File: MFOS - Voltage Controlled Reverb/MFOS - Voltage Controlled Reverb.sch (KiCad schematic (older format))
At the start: 94 parts, among them J1 X6, J10 X5, J11 GND_Conn, J12 +12V_Conn, J13 -12V_Conn, J14 X4, J2 X9, J3 X10, J4 X7, J5 X8, J6 X11, J7 X1, J8 X2, J9 X3, Q1 2N3906, Q2 2N3906, U1 LM386, U2 LF411, U3 TL074, U4 LM13700, U5 TL072, U6 TL072

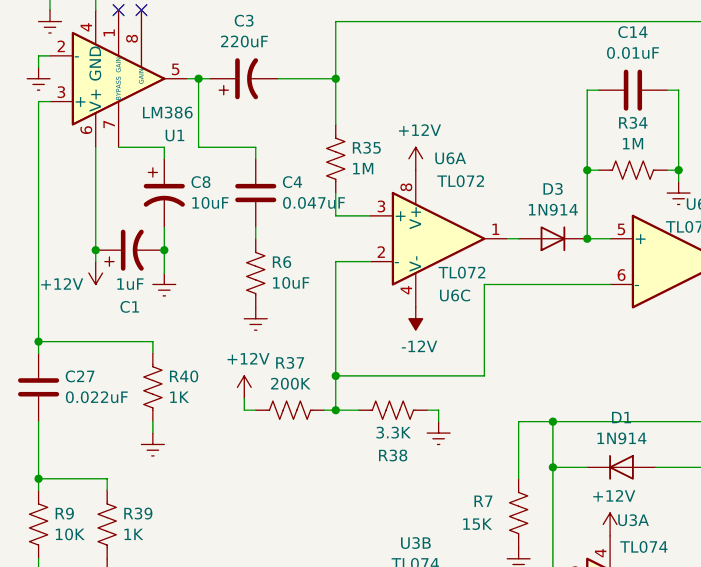
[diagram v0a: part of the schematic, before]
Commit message: placed components on pcb, some caps i think have the wrong footprint
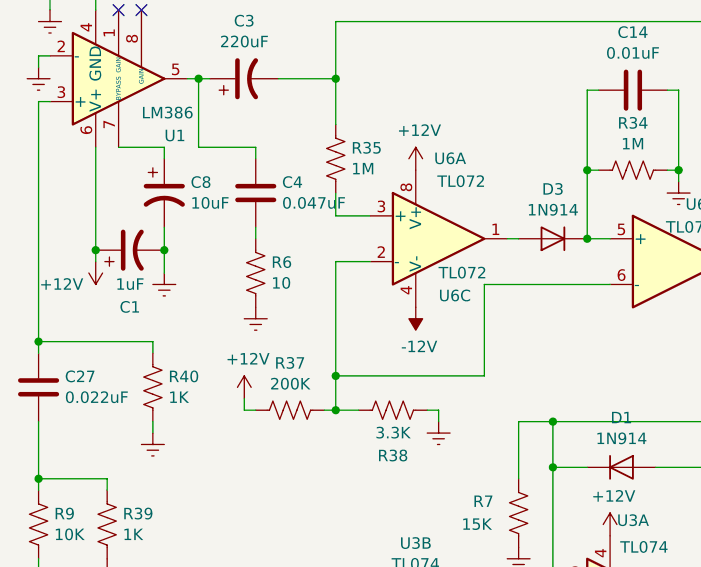
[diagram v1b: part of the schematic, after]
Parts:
- Q1, Q2: footprint Package_TO_SOT_THT:TO-92_Inline -> Package_TO_SOT_THT:TO-92_Inline_Wide
- R6: value 10uF -> 10
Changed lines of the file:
@@
 P 1650 1850
 F 0 "R6" H 1718 1896 50  0000 L CNN
-F 1 "10uF" H 1718 1805 50  0000 L CNN
+F 1 "10" H 1718 1805 50  0000 L CNN
 F 2 "Resistor_THT:R_Axial_DIN0207_L6.3mm_D2.5mm_P7.62mm_Horizontal" V 1690 1840 50  0001 C CNN
 F 3 "~" H 1650 1850 50  0001 C CNN
@@
 F 0 "Q1" H 4140 3254 50  0000 L CNN
 F 1 "2N3906" H 4140 3345 50  0000 L CNN
-F 2 "Package_TO_SOT_THT:TO-92_Inline" H 4150 3225 50  0001 L CIN
+F 2 "Package_TO_SOT_THT:TO-92_Inline_Wide" H 4150 3225 50  0001 L CIN
 F 3 "https://www.fairchildsemi.com/datasheets/2N/2N3906.pdf" H 3950 3300 50  0001 L CNN
 	1    3950 3300
@@
 F 0 "Q2" H 5090 6404 50  0000 L CNN
 F 1 "2N3906" H 5090 6495 50  0000 L CNN
-F 2 "Package_TO_SOT_THT:TO-92_Inline" H 5100 6375 50  0001 L CIN
+F 2 "Package_TO_SOT_THT:TO-92_Inline_Wide" H 5100 6375 50  0001 L CIN
 F 3 "https://www.fairchildsemi.com/datasheets/2N/2N3906.pdf" H 4900 6450 50  0001 L CNN
 	1    4900 6450

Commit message: progress on wiring
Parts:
- C1, C10, C11, C12, C13: footprint Capacitor_THT:C_Rect_L7.0mm_W2.5mm_P5.00mm -> Capacitor_THT:CP_Radial_D5.0mm_P2.50mm
- C26, C6, C7, C8, C9: footprint Capacitor_THT:CP_Radial_D8.0mm_P3.50mm -> Capacitor_THT:CP_Radial_D6.3mm_P2.50mm
- C3: footprint Capacitor_THT:C_Rect_L7.0mm_W2.5mm_P5.00mm -> Capacitor_THT:CP_Radial_D6.3mm_P2.50mm
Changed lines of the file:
@@
 F 0 "C1" V 850 1750 50  0000 C CNN
 F 1 "1uF" V 950 1750 50  0000 C CNN
-F 2 "Capacitor_THT:C_Rect_L7.0mm_W2.5mm_P5.00mm" H 1100 1750 50  0001 C CNN
+F 2 "Capacitor_THT:CP_Radial_D5.0mm_P2.50mm" H 1100 1750 50  0001 C CNN
 F 3 "~" H 1100 1750 50  0001 C CNN
 	1    1100 1750
@@
 F 0 "C3" V 1852 1000 50  0000 C CNN
 F 1 "220uF" V 1761 1000 50  0000 C CNN
-F 2 "Capacitor_THT:C_Rect_L7.0mm_W2.5mm_P5.00mm" H 1600 1000 50  0001 C CNN
+F 2 "Capacitor_THT:CP_Radial_D6.3mm_P2.50mm" H 1600 1000 50  0001 C CNN
 F 3 "~" H 1600 1000 50  0001 C CNN
 	1    1600 1000
@@
 F 0 "C10" V 6198 3950 50  0000 C CNN
 F 1 "1uF" V 6289 3950 50  0000 C CNN
-F 2 "Capacitor_THT:C_Rect_L7.0mm_W2.5mm_P5.00mm" H 6450 3950 50  0001 C CNN
+F 2 "Capacitor_THT:CP_Radial_D5.0mm_P2.50mm" H 6450 3950 50  0001 C CNN
 F 3 "~" H 6450 3950 50  0001 C CNN
 	1    6450 3950
@@
 F 0 "C12" V 6198 4350 50  0000 C CNN
 F 1 "1uF" V 6289 4350 50  0000 C CNN
-F 2 "Capacitor_THT:C_Rect_L7.0mm_W2.5mm_P5.00mm" H 6450 4350 50  0001 C CNN
+F 2 "Capacitor_THT:CP_Radial_D5.0mm_P2.50mm" H 6450 4350 50  0001 C CNN
 F 3 "~" H 6450 4350 50  0001 C CNN
 	1    6450 4350
@@
 F 0 "C9" V 7748 3850 50  0000 C CNN
 F 1 "10uF" V 7839 3850 50  0000 C CNN
-F 2 "Capacitor_THT:CP_Radial_D8.0mm_P3.50mm" H 8000 3850 50  0001 C CNN
+F 2 "Capacitor_THT:CP_Radial_D6.3mm_P2.50mm" H 8000 3850 50  0001 C CNN
 F 3 "~" H 8000 3850 50  0001 C CNN
 	1    8000 3850
@@
 F 0 "C8" H 1365 1546 50  0000 L CNN
 F 1 "10uF" H 1365 1455 50  0000 L CNN
-F 2 "Capacitor_THT:CP_Radial_D8.0mm_P3.50mm" H 1250 1500 50  0001 C CNN
+F 2 "Capacitor_THT:CP_Radial_D6.3mm_P2.50mm" H 1250 1500 50  0001 C CNN
 F 3 "~" H 1250 1500 50  0001 C CNN
 	1    1250 1500
@@
 F 0 "C7" V 9450 5750 50  0000 C CNN
 F 1 "220uF" V 9550 5750 50  0000 C CNN
-F 2 "Capacitor_THT:CP_Radial_D8.0mm_P3.50mm" H 9700 5750 50  0001 C CNN
+F 2 "Capacitor_THT:CP_Radial_D6.3mm_P2.50mm" H 9700 5750 50  0001 C CNN
 F 3 "~" H 9700 5750 50  0001 C CNN
 	1    9700 5750
@@
 F 0 "C6" V 8000 5750 50  0000 C CNN
 F 1 "220uF" V 8100 5750 50  0000 C CNN
-F 2 "Capacitor_THT:CP_Radial_D8.0mm_P3.50mm" H 8250 5750 50  0001 C CNN
+F 2 "Capacitor_THT:CP_Radial_D6.3mm_P2.50mm" H 8250 5750 50  0001 C CNN
 F 3 "~" H 8250 5750 50  0001 C CNN
 	1    8250 5750
@@
 F 0 "C13" V 1398 7300 50  0000 C CNN
 F 1 "1uF" V 1489 7300 50  0000 C CNN
-F 2 "Capacitor_THT:C_Rect_L7.0mm_W2.5mm_P5.00mm" H 1688 7150 50  0001 C CNN
+F 2 "Capacitor_THT:CP_Radial_D5.0mm_P2.50mm" H 1688 7150 50  0001 C CNN
 F 3 "~" H 1650 7300 50  0001 C CNN
 	1    1650 7300
@@
 F 0 "C11" H 1935 5604 50  0000 R CNN
 F 1 "1uF" H 1935 5695 50  0000 R CNN
-F 2 "Capacitor_THT:C_Rect_L7.0mm_W2.5mm_P5.00mm" H 2088 5500 50  0001 C CNN
+F 2 "Capacitor_THT:CP_Radial_D5.0mm_P2.50mm" H 2088 5500 50  0001 C CNN
 F 3 "~" H 2050 5650 50  0001 C CNN
 	1    2050 5650
@@
 F 0 "C26" H 10565 2046 50  0000 L CNN
 F 1 "10uF" H 10565 1955 50  0000 L CNN
-F 2 "Capacitor_THT:CP_Radial_D8.0mm_P3.50mm" H 10450 2000 50  0001 C CNN
+F 2 "Capacitor_THT:CP_Radial_D6.3mm_P2.50mm" H 10450 2000 50  0001 C CNN
 F 3 "~" H 10450 2000 50  0001 C CNN
 	1    10450 2000

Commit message: wuw
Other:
- note added: "R40 should be 100k"
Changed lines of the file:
@@
 NoConn ~ 5050 7200
 NoConn ~ 950  7100
+Text Notes 1150 2700 0    50   ~ 0
+R40 should be 100k
 $EndSCHEMATC
